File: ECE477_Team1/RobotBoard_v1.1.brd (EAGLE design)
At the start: 101.6 x 81.3 mm, 86 parts, among them IC1L A3967SLB, IC1R A3967SLB, IC33 3.3, IC5 5

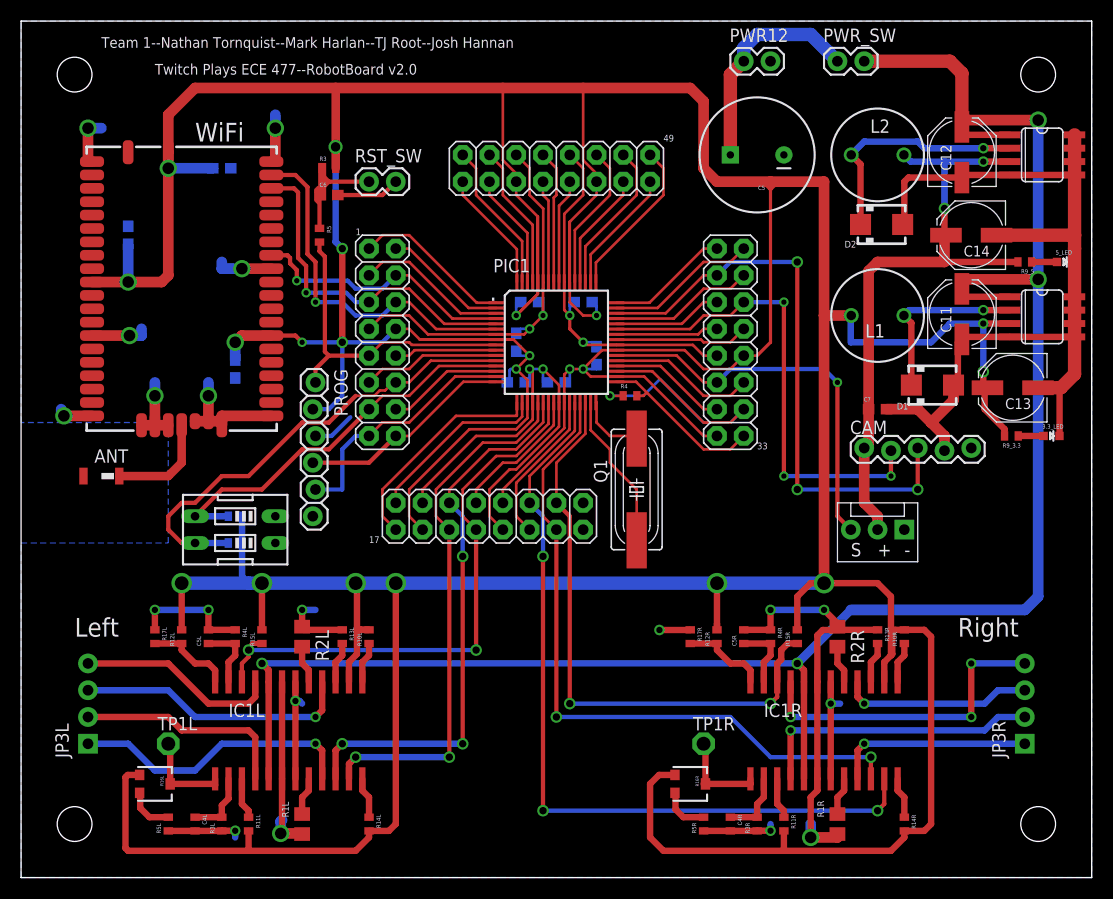
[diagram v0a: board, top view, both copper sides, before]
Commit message: Updated Power Regulators and created v2.0
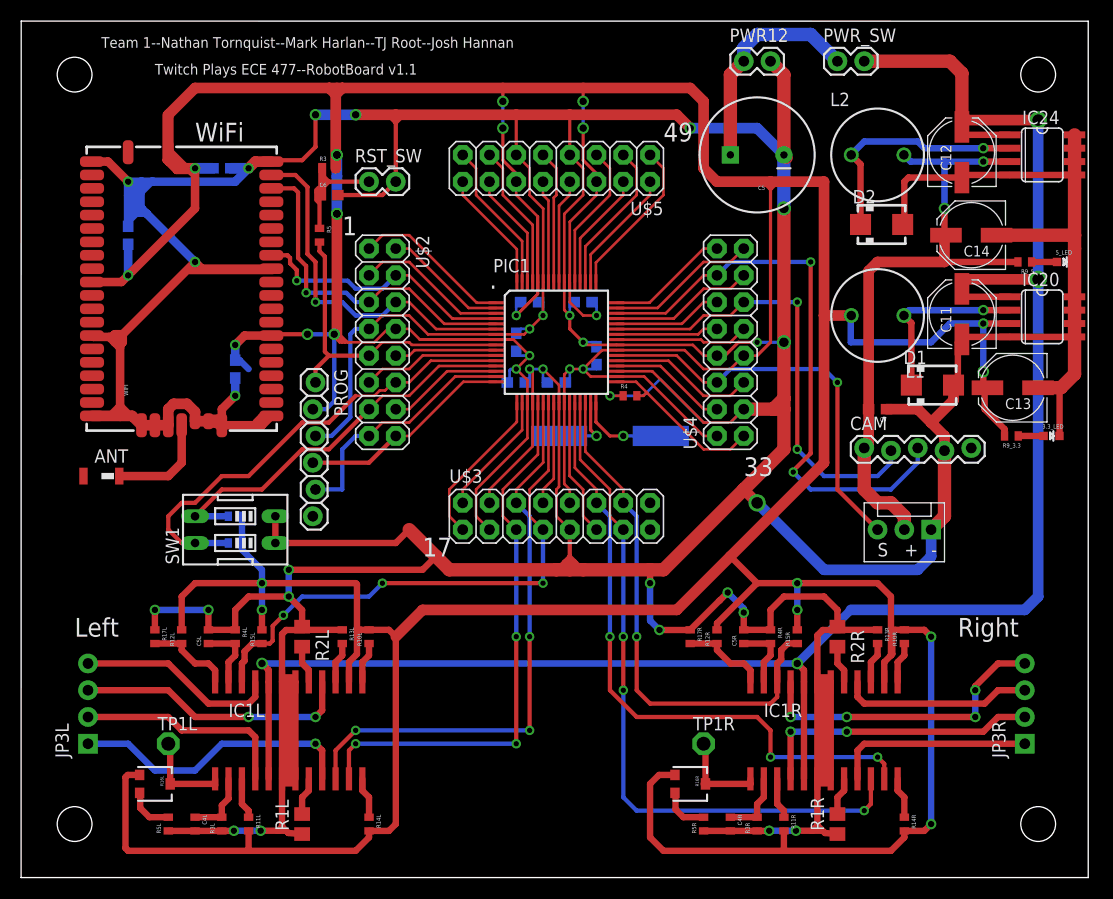
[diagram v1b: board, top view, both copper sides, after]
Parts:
- IC20: value 3.3 -> AP1509-33
- IC24: value 5 -> AP1509-5
- moved U$3 6.35 mm to (41.9, 33.0)
- moved Q1 5.68 mm to (55.9, 41.9), flipped to the bottom, turned to 180 degrees
- moved PAD 2.54 mm to (86.4, 33.0)
- renumbered IC33 to IC20, IC5 to IC24
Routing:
- net GND: track 405.2 -> 738.9 mm, vias 26 -> 30
- net N$31: track 0.00 -> 18.0 mm, vias 0 -> 2
- net TDI: track 76.1 -> 60.5 mm
- net 3.3V: track 659.6 -> 671.7 mm, vias 21 -> 25
- net N$6: track 14.9 -> 6.98 mm, vias 0 -> 1
- net N$30: track 0.00 -> 7.89 mm
- net N$27: track 0.00 -> 7.87 mm
- net RB15: track 56.6 -> 49.9 mm, vias 2 -> 1
- net RB6: track 21.2 -> 15.3 mm
- net RB7: track 17.5 -> 11.9 mm
- net TDD: track 13.3 -> 9.96 mm
- net TMS: track 56.0 -> 53.3 mm, vias 2 -> 3
- net RD9: track 46.0 -> 43.8 mm, vias 3 -> 2
- net N$15: track 6.42 -> 8.57 mm, vias 0 -> 1
- net RB8: track 51.3 -> 53.1 mm, vias 2 -> 3
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- removed copper zone on layer 16, net GND
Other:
- board size 101.6 x 81.3 mm -> 101.3 x 81.3 mm
- board text added: "Twitch Plays ECE 477--RobotBoard v1.1"
- board text removed: "Twitch Plays ECE 477--RobotBoard v2.0"
